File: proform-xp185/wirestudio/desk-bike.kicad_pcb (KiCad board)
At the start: 2 copper layers, 152.3 x 163.3 mm, 23 parts, among them J1 Motor, M1 esp32-devkitc-v4, Q1 IRF4905, Q2 IRFZ44N, Q3 2N3904, Q4 IRF4905, Q5 IRFZ44N, Q6 2N3904, U1 SSD1306, U2 Rotary encoder, U3 Input, U4 Input, U5 Input, U6 ADC sense, U7 Pulse source

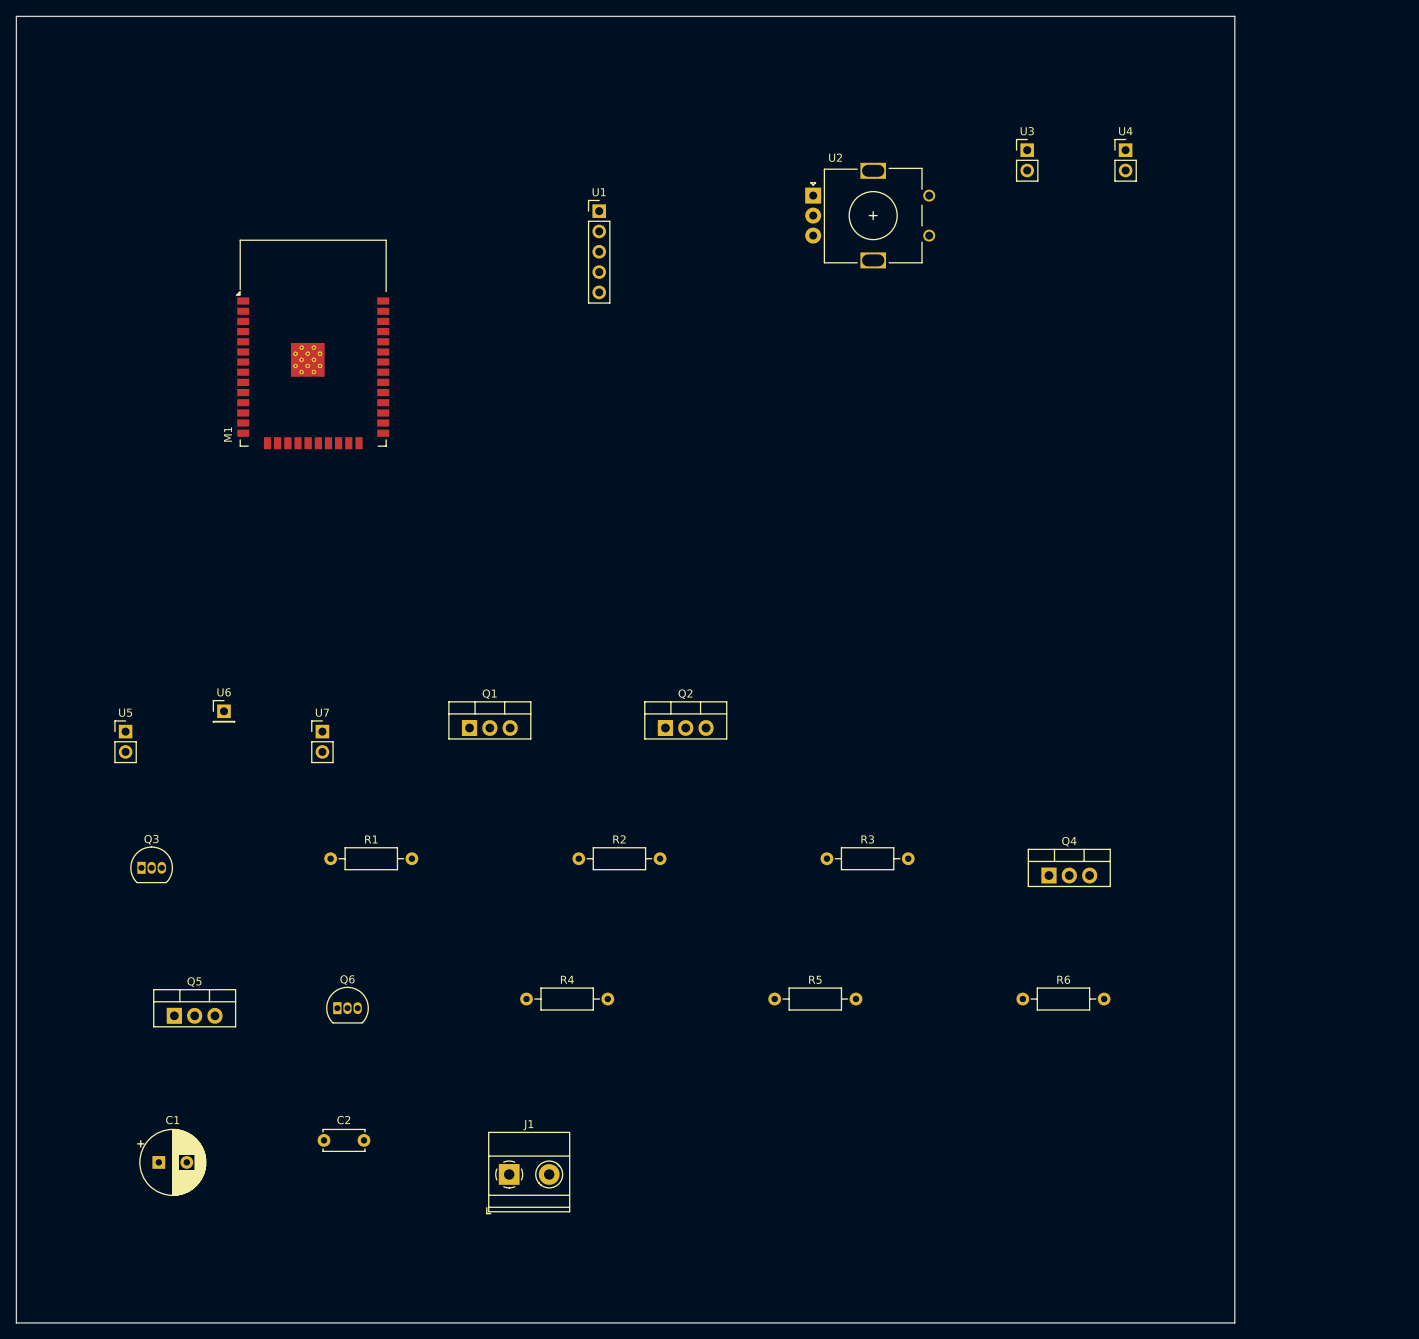
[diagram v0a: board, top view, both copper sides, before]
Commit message: WireStudio: routed board, CPL and JLCPCB fab bundle
Autorouted on the studio (Freerouting via wirestudio 0.38.0): all 28
nets, 118 segments, 5 vias. desk-bike-fab.zip is the upload bundle from
the routed board (Gerbers, drill, BOM, CPL). README points at the
usb_c_power_in library part (WireStudio#298) and the connector proposal
(WireStudio#300) for what is still added by hand.

Co-Authored-By: Claude Fable 5.1 <noreply@anthropic.com>
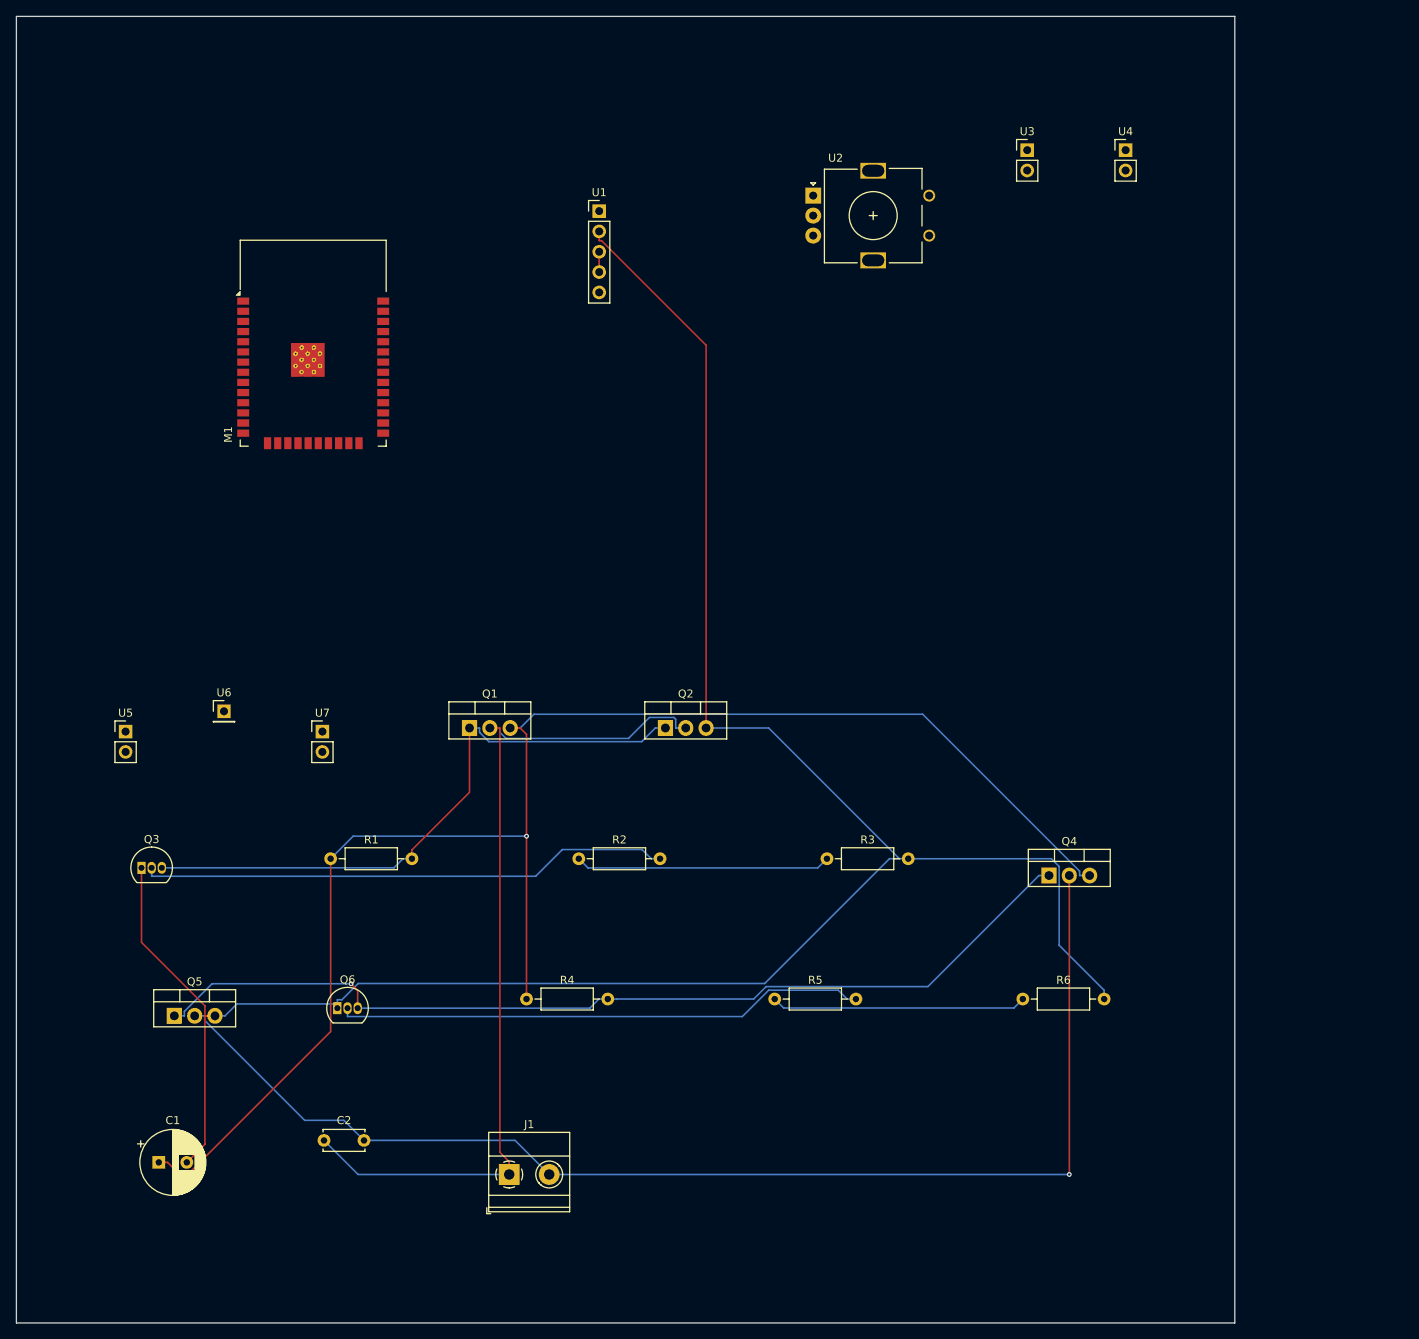
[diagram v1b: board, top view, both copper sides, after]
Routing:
- net GND: track 0.00 -> 276.1 mm
- net +5V: track 0.00 -> 193.7 mm, vias 0 -> 1
- net bridge_out_b: track 0.00 -> 155.2 mm, vias 0 -> 1
- net bridge_gate_b: track 0.00 -> 120.7 mm, vias 0 -> 1
- net bridge_out_a: track 0.00 -> 110.1 mm
- net bridge_gate_a: track 0.00 -> 77.3 mm
- net bridge_base_a: track 0.00 -> 66.5 mm
- net bridge_base_b: track 0.00 -> 66.4 mm
- net GPIO_GPIO18: track 0.00 -> 32.0 mm
- net GPIO_GPIO19: track 0.00 -> 31.9 mm
- net BUS_i2c0: track 0.00 -> 2.54 mm

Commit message: WireStudio: USB-C 5 V input on the board, re-routed, new fab bundle
The usb_c_power_in library part shipped in WireStudio 0.39.0, so the
design now carries a psu instance (J2 receptacle, R7/R8 5.1k CC
pull-downs, C3 10 uF) feeding the 5 V rail. Saved to the studio through
the new create_design MCP tool. Re-routed: 39 nets, 179 segments,
7 vias, nothing unrouted. BOM, CPL, wiring, SKiDL script and the JLCPCB
bundle regenerated from it.

Co-Authored-By: Claude Fable 5.1 <noreply@anthropic.com>
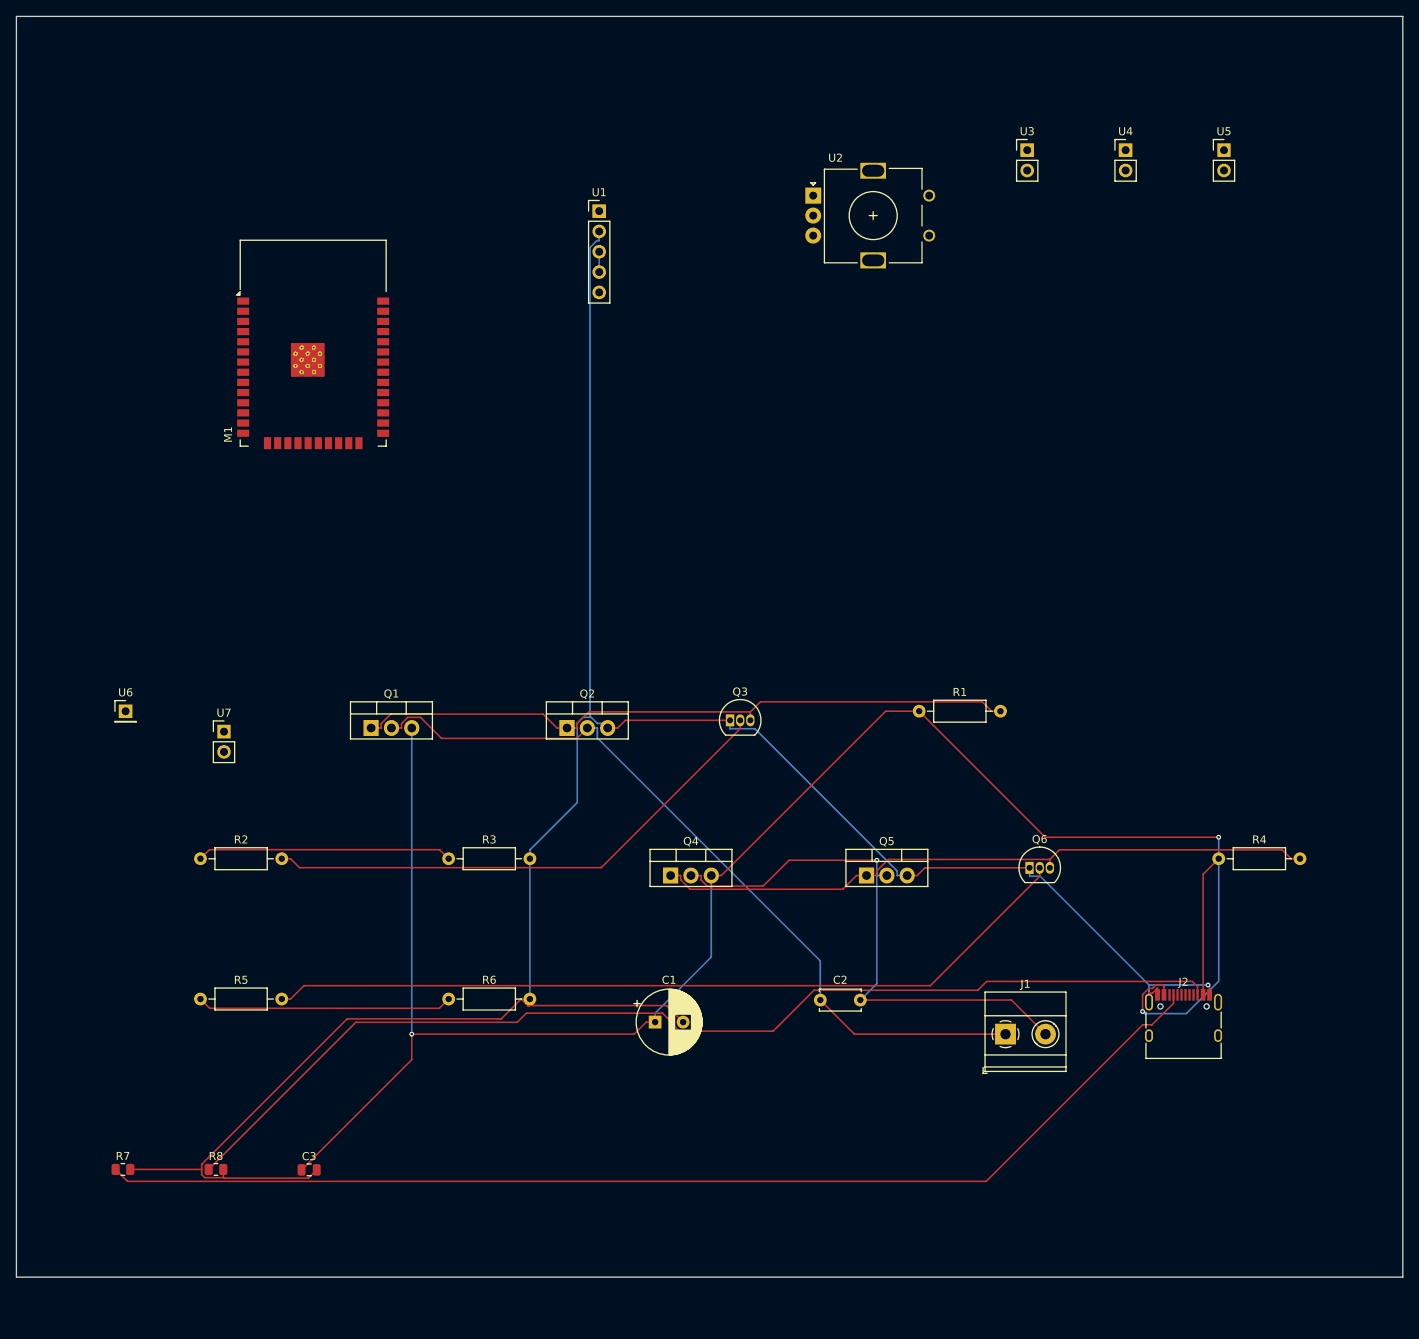
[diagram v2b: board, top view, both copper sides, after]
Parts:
- added C3: 10uF, Capacitor_SMD:C_0805_2012Metric, F.Cu at (52.0, 159.6)
- added J2: USB-C, Connector_USB:USB_C_Receptacle_HRO_TYPE-C-31-M-12, F.Cu at (161.3, 141.8)
- added R7: 5.1k, Resistor_SMD:R_0805_2012Metric, F.Cu at (28.7, 159.5)
- added R8: 5.1k, Resistor_SMD:R_0805_2012Metric, F.Cu at (40.3, 159.5)
- moved U5 155.4 mm to (166.3, 32.1)
- moved Q5 88.3 mm to (121.7, 122.8)
- moved R4 88.3 mm to (165.7, 120.7)
- moved Q6 88.3 mm to (142.0, 121.8)
- moved Q3 75.8 mm to (104.6, 103.4)
- moved R1 75.8 mm to (128.2, 102.2)
- moved R5 71.8 mm to (38.4, 138.2)
- moved R6 71.8 mm to (69.4, 138.2)
- moved C1 64.5 mm to (95.2, 141.1)
- moved C2 64.5 mm to (115.9, 138.4)
- moved J1 64.5 mm to (139.0, 142.6)
- moved R2 47.3 mm to (38.4, 120.7)
- moved Q4 47.3 mm to (97.2, 122.8)
- moved R3 47.3 mm to (69.4, 120.7)
- moved Q1 12.3 mm to (59.7, 104.3)
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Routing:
- net psu_cc1: track 0.00 -> 143.1 mm
- net psu_cc2: track 0.00 -> 136.6 mm
- net bridge_out_b: track 155.2 -> 69.9 mm
- net +5V: track 193.7 -> 245.2 mm, vias 1 -> 3
- net bridge_gate_b: track 120.7 -> 83.6 mm, vias 1 -> 0
- net bridge_base_b: track 66.4 -> 102.2 mm
- net GND: track 276.1 -> 298.6 mm, vias 0 -> 1
- net bridge_out_a: track 110.1 -> 98.7 mm
- net bridge_gate_a: track 77.3 -> 83.6 mm
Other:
- board size 152.3 x 163.3 mm -> 173.3 x 157.6 mm
